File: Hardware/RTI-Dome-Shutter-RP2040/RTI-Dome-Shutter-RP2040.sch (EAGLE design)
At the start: 107 parts, among them IC2 24LC64T-I/SN, IC3 FT232RL, IC4 RASPBERRY_PI_PICO, IC8 REG1117-3.3V, IC9 REG1117-5V, J2 XT60PW-M, U1 W5500, X13 PN61729-S, X9 J1011F21PNL

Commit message: New RP2040 shutter board
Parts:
- removed 25MHZ: CB3LV-OSCILATOR, rti:CB3LV-OSCILATOR
- removed C10: 22nF, rcl:C-EUC0805
- removed C11, C12, C14, C16, C17, C20, C8, C9: 100nF, rcl:C-EUC0805
- removed C13, C18, C22: 10nF, rcl:C-EUC0805
- removed C15, C21: 6.8nF, rcl:C-EUC0805
- removed C19: 4.7uF, rcl:C-EUC0805
- removed FL1: BLM21AG121SN1D, BLM21AG121SN1D:BLM21AG121SN1D
- removed IC3: FT232RL, ftdichip:FT232RL
- removed R11: 10K, rcl:R-EU_R0805
- removed R23: 10 1%, rcl:R-EU_R0805
- removed R24, R25, R26, R27: 49.9 1%, rcl:R-EU_R0805
- removed R28, R29: 330, rcl:R-EU_R0805
- removed R30, R31, R32, R33, R34, R35, R36, R37, R38, R40: 4.7K, rcl:R-EU_R0805
- removed R39: 12.4K 1%, rcl:R-EU_R0805
- removed U$2: MCP120T, MCP120T:MCP120T
- removed U1: W5500, W5500:W5500
- removed X13: PN61729-S, rti:PN61729-S
- removed X9: J1011F21PNL, rti:J1011F21PNL
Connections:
- removed net ACT_LED: U1.ACTLED, X9.C-L
- removed net AVDD: C11.1, C12.1, C14.1, C17.1, FL1.1, R23.2, R24.2, R25.2, U1.AVDD@1, U1.AVDD@2, U1.AVDD@3, U1.AVDD@4, U1.AVDD@5, U1.AVDD@6
- removed net DTR_DSR_DCD: IC3.!DCD, IC3.!DSR, IC3.!DTR
- removed net INT_N: U1.INT_N
- removed net LINK_ACK: U1.LINKLED, X9.C-R
- removed net N$10: R28.1, X9.AL
- removed net N$11: C15.2, X9.RD+
- removed net N$12: C21.2, X9.RD-
- removed net N$13: C10.1, R23.1, X9.CT
- removed net N$17: U1.DUPLED
- removed net N$22: R31.1, U1.RSVD@2
- removed net N$23: R32.1, U1.RSVD@3
- removed net N$24: R33.1, U1.RSVD@4
- removed net N$25: R34.1, U1.RSVD@5
- removed net N$26: R35.1, U1.RSVD@6
- removed net N$27: R36.1, U1.PMODE2
- removed net N$28: R37.1, U1.PMODE1
- removed net N$29: R38.1, U1.PMODE0
- removed net N$31: C19.2, U1.TOCAP
- removed net N$32: U1.VBG
- removed net N$33: C18.2, U1.1V2O
- removed net N$34: R39.1, U1.EXRES1
- removed net N$35: R40.2, U1.RSVD@1
- removed net N$6: C8.1, IC3.3V3OUT
- removed net N$7: C22.1, R26.2, R27.2, X9.CR
- removed net N$8: R29.1, X9.A-R
- removed net RTS_CTS: IC3.!CTS, IC3.!RTS
- removed net RXN: C21.1, R26.1, U1.RXN
- removed net RXP: C15.1, R27.1, U1.RXP
- removed net TXN: R25.1, U1.TXN, X9.TD-
- removed net TXP: R24.1, U1.TXP, X9.TD+
- removed net USBD_N: IC3.USBDM, X13.2
- removed net USBD_P: IC3.USBDP, X13.3
- removed net USB_VCC: X13.1
- removed net XI: 25MHZ.FO, U1.XI/CLKIN
- removed net XO: U1.XO
- net 3.3V: no longer 25MHZ.OE, 25MHZ.VDD, C13.1, C16.1, C20.1, C9.1, FL1.2, IC3.VCCIO, R28.2, R29.2, R30.2, R36.2, R37.2, R38.2, U$2.VDD, U1.VDD
- net ETH_CS: no longer U1.SCS_N
- net ETH_RESET: no longer R30.1, U1.RST_N
- net FTDI_RESET: no longer IC3.!RESET, R11.1
- net GND: no longer 25MHZ.GND, C10.2, C11.2, C12.2, C13.2, C14.2, C16.2, C17.2, C18.1, C19.1, C20.2, C22.2, C8.2, C9.2, IC3.GND, IC3.GND@1, IC3.GND@2, IC3.GND@A, R11.2, R31.2, R32.2, R33.2, R34.2, R35.2, R39.2, R40.1, U$2.VSS, U1.AGND@1, U1.AGND@2, U1.AGND@3, U1.AGND@4, U1.AGND@5, U1.AGND@6, U1.GND, X13.4, X13.S1, X13.S2, X9.4/NC, X9.5/NC, X9.CGND, X9.CGND2
- net RESET: no longer U$2.~RST
- net RX2: no longer IC3.TXD
- net SCLK: no longer U1.SCLK
- net SDI: no longer U1.MISO
- net SDO: no longer U1.MOSI
- net TX2: no longer IC3.RXD
- net VCC: no longer IC3.VCC

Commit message: Switching to 0603 for resistor and capacitors
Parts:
- removed C7: 100nF, rcl:C-EUC0805
- C1, C23, C24, C27, C28, C3, C4, C40, C42, C43, C44, C45, C46, C5, C6: device rcl:C-EUC0805 -> rcl:C-EUC0603
- R1, R10, R12, R15, R16, R17, R18, R2, R20, R21, R22, R3, R4, R41, R44, R45, R46, R47, R49, R5, R50, R6, R7, R8, R9: device rcl:R-EU_R0805 -> rcl:R-EU_R0603
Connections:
- net GND: no longer C7.2
- net VCC: no longer C7.1

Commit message: Routed RP2040 Shutter board
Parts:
- C1, C23, C24, C27, C28, C3, C4, C40, C42, C43, C44, C45, C46, C5, C6: device rcl:C-EUC0603 -> rti:C-EU'0603'
- C41: device rcl:C-EUC0805 -> rti:C-EU'0603'
- IC2: device Microchip_By_element14_Batch_1:24LC64T-I/SN -> rti:24LC64T-I/SN
- R1, R10, R12, R15, R16, R17, R18, R2, R20, R21, R22, R3, R4, R41, R44, R45, R46, R47, R49, R5, R50, R6, R7, R8, R9: device rcl:R-EU_R0603 -> rti:R-EU'0603'
- R48: device rcl:R-EU_R0805 -> rti:R-EU'0603'

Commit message: Removed XBee from RP2040 Shutter controller
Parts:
- removed XB1: XBEE, rti:XBEE
- added Q1: DMG2305UX-7, samacsys:DMG2305UX-7
- added S1: EVQ-P2H02B, samacsys:EVQ-P2H02B
- IC4: value RASPBERRY_PI_PICO -> RASPBERRY_PI_PICOW; device samacsys:RASPBERRY_PI_PICO -> samacsys:RASPBERRY_PI_PICOW; DESCRIPTION RASPBERRY-PI - RASPBERRY PI PICO - Raspberry Pi Board, Rasp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 -> (none); MANUFACTURER_NAME RASPBERRY-PI PICO -> (none); MANUFACTURER_PART_NUMBER SC0916 -> (none); MOUSER_PART_NUMBER SC0915 -> (none); MPN SC0916 -> (none)
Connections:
- removed net N$64: IC4.VBUS
- removed net N$9: XB1.!CTS!/DIO7, XB1.!RTS!/AD6/DIO6
- new net VBUS: IC4.VBUS, Q1.G
- new net VSYS: IC4.VSYS, Q1.S
- net 3.3V: no longer XB1.VCC
- net GND: now also S1.COM_1, S1.COM_2; no longer XB1.!DTR!/SLEEP_RQ/DI8, XB1.GND
- net RESET: now also S1.NO_2
- net VCC: now also Q1.D; no longer IC4.VSYS
- net XBEE_DIN: no longer XB1.DIN/!CONFIG
- net XBEE_DOUT: no longer XB1.DOUT
- net XBEE_RESET: no longer XB1.!RESET

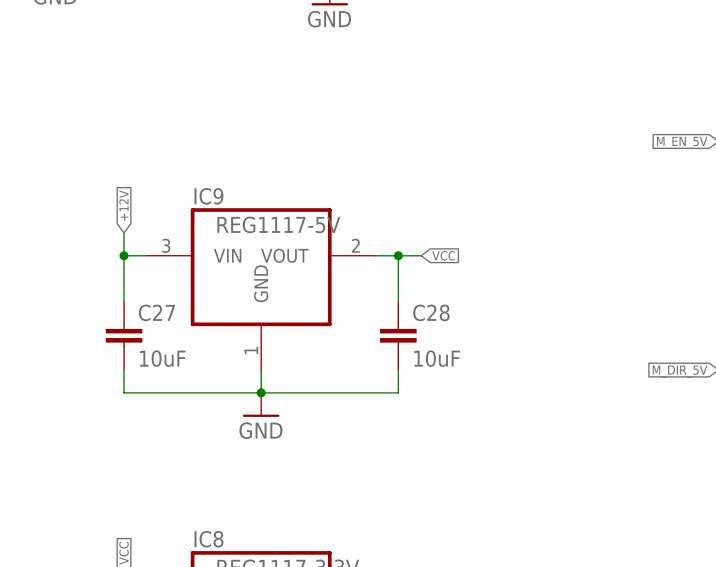
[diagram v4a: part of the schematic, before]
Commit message: Removed XBee from RP2040 boards as they'll use WiFi
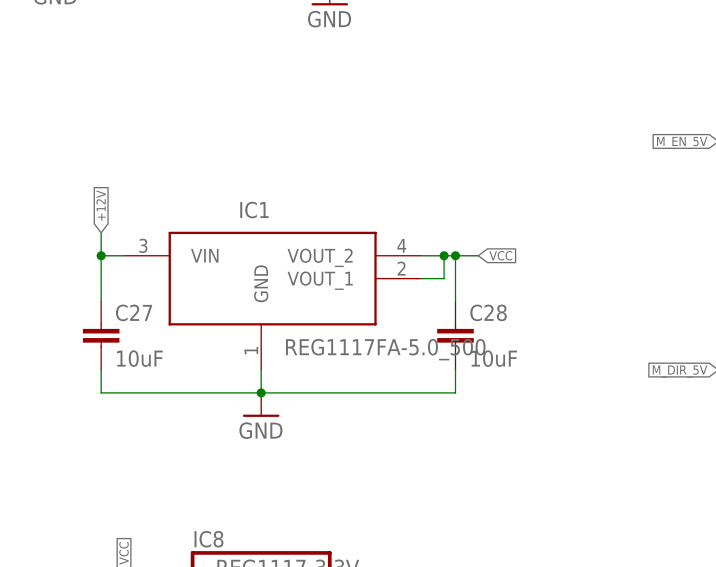
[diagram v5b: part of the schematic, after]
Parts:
- removed IC9: REG1117-5V, burr-brown:REG1117
- added IC1: REG1117FA-5.0_500, REG1117FA-5.0_500:REG1117FA-5.0_500
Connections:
- net +12V: now also IC1.VIN; no longer IC9.VIN
- net GND: now also IC1.GND; no longer IC9.GND
- net VCC: now also IC1.VOUT_1, IC1.VOUT_2; no longer IC9.VOUT
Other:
- moved on the sheet: C27, C28
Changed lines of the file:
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@@
 </part>
 <part name="GND22" library="supply1" library_urn="urn:adsk.eagle:library:371" deviceset="GND" device=""/>
-<part name="IC9" library="burr-brown" library_urn="urn:adsk.eagle:library:37504555" deviceset="REG1117" device="" package3d_urn="urn:adsk.eagle:package:37504714/1" value="REG1117-5V">
-<attribute name="MPN" value="REG1117-3.3/2K5"/>
-</part>
 <part name="C27" library="rti" library_urn="urn:adsk.eagle:library:37256580" deviceset="C-EU" device="'0603'" package3d_urn="urn:adsk.eagle:package:41513588/2" value="10uF">
 <spice>
@@
 <part name="S1" library="samacsys" library_urn="urn:adsk.eagle:library:37256869" deviceset="EVQ-P2H02B" device="" package3d_urn="urn:adsk.eagle:package:44159643/2"/>
 <part name="GND3" library="supply1" library_urn="urn:adsk.eagle:library:371" deviceset="GND" device=""/>
+<part name="IC1" library="REG1117FA-5.0_500" library_urn="urn:adsk.eagle:library:43937876" deviceset="REG1117FA-5.0_500" device="" package3d_urn="urn:adsk.eagle:package:43937879/3"/>
 </parts>
 <sheets>
@@
 <attribute name="VALUE" x="27.94" y="93.98" size="1.778" layer="96"/>
 </instance>
-<instance part="IC9" gate="G$1" x="30.48" y="152.4" smashed="yes">
-<attribute name="NAME" x="22.86" y="158.115" size="1.778" layer="95" ratio="10"/>
-<attribute name="VALUE" x="25.4" y="154.94" size="1.778" layer="96" ratio="10"/>
-</instance>
-<instance part="C27" gate="G$1" x="15.24" y="144.78" smashed="yes">
-<attribute name="MPN" x="15.24" y="144.78" size="1.778" layer="96" display="off"/>
-<attribute name="NAME" x="16.764" y="145.161" size="1.778" layer="95"/>
-<attribute name="VALUE" x="16.764" y="140.081" size="1.778" layer="96"/>
-</instance>
-<instance part="C28" gate="G$1" x="45.72" y="144.78" smashed="yes">
-<attribute name="MPN" x="45.72" y="144.78" size="1.778" layer="96" display="off"/>
-<attribute name="NAME" x="47.244" y="145.161" size="1.778" layer="95"/>
-<attribute name="VALUE" x="47.244" y="140.081" size="1.778" layer="96"/>
+<instance part="C27" gate="G$1" x="12.7" y="144.78" smashed="yes">
+<attribute name="MPN" x="12.7" y="144.78" size="1.778" layer="96" display="off"/>
+<attribute name="NAME" x="14.224" y="145.161" size="1.778" layer="95"/>
+<attribute name="VALUE" x="14.224" y="140.081" size="1.778" layer="96"/>
+</instance>
+<instance part="C28" gate="G$1" x="52.07" y="144.78" smashed="yes">
+<attribute name="MPN" x="52.07" y="144.78" size="1.778" layer="96" display="off"/>
+<attribute name="NAME" x="53.594" y="145.161" size="1.778" layer="95"/>
+<attribute name="VALUE" x="53.594" y="140.081" size="1.778" layer="96"/>
 </instance>
 <instance part="GND23" gate="1" x="30.48" y="134.62" smashed="yes">
@@
 <instance part="GND3" gate="1" x="219.71" y="30.48" smashed="yes">
 <attribute name="VALUE" x="217.17" y="27.94" size="1.778" layer="96"/>
+</instance>
+<instance part="IC1" gate="G$1" x="15.24" y="152.4" smashed="yes">
+<attribute name="NAME" x="27.94" y="157.48" size="1.778" layer="95" align="center-left"/>
+<attribute name="VALUE" x="33.02" y="142.24" size="1.778" layer="96" align="center-left"/>
 </instance>
 </instances>
@@
 </segment>
 <segment>
-<pinref part="IC9" gate="G$1" pin="GND"/>
 <wire x1="30.48" y1="137.16" x2="30.48" y2="139.7" width="0.1524" layer="91"/>
 <pinref part="C28" gate="G$1" pin="2"/>
-<wire x1="45.72" y1="139.7" x2="45.72" y2="137.16" width="0.1524" layer="91"/>
-<wire x1="45.72" y1="137.16" x2="30.48" y2="137.16" width="0.1524" layer="91"/>
+<wire x1="52.07" y1="139.7" x2="52.07" y2="137.16" width="0.1524" layer="91"/>
+<wire x1="52.07" y1="137.16" x2="30.48" y2="137.16" width="0.1524" layer="91"/>
 <junction x="30.48" y="137.16"/>
 <pinref part="C27" gate="G$1" pin="2"/>
-<wire x1="15.24" y1="139.7" x2="15.24" y2="137.16" width="0.1524" layer="91"/>
-<wire x1="15.24" y1="137.16" x2="30.48" y2="137.16" width="0.1524" layer="91"/>
+<wire x1="12.7" y1="139.7" x2="12.7" y2="137.16" width="0.1524" layer="91"/>
+<wire x1="12.7" y1="137.16" x2="30.48" y2="137.16" width="0.1524" layer="91"/>
 <pinref part="GND23" gate="1" pin="GND"/>
+<pinref part="IC1" gate="G$1" pin="GND"/>
 </segment>
 <segment>
@@
 <segment>
 <pinref part="C27" gate="G$1" pin="1"/>
-<pinref part="IC9" gate="G$1" pin="VIN"/>
-<wire x1="15.24" y1="147.32" x2="15.24" y2="152.4" width="0.1524" layer="91"/>
-<wire x1="15.24" y1="152.4" x2="17.78" y2="152.4" width="0.1524" layer="91"/>
-<wire x1="15.24" y1="154.94" x2="15.24" y2="152.4" width="0.1524" layer="91"/>
-<junction x="15.24" y="152.4"/>
-<label x="15.24" y="154.94" size="1.016" layer="95" rot="R90" xref="yes"/>
+<wire x1="12.7" y1="147.32" x2="12.7" y2="152.4" width="0.1524" layer="91"/>
+<wire x1="12.7" y1="152.4" x2="15.24" y2="152.4" width="0.1524" layer="91"/>
+<wire x1="12.7" y1="154.94" x2="12.7" y2="152.4" width="0.1524" layer="91"/>
+<junction x="12.7" y="152.4"/>
+<label x="12.7" y="154.94" size="1.016" layer="95" rot="R90" xref="yes"/>
+<pinref part="IC1" gate="G$1" pin="VIN"/>
 </segment>
 </net>
@@
 </segment>
 <segment>
-<pinref part="IC9" gate="G$1" pin="VOUT"/>
 <pinref part="C28" gate="G$1" pin="1"/>
-<wire x1="43.18" y1="152.4" x2="45.72" y2="152.4" width="0.1524" layer="91"/>
-<wire x1="45.72" y1="152.4" x2="45.72" y2="147.32" width="0.1524" layer="91"/>
-<wire x1="48.26" y1="152.4" x2="45.72" y2="152.4" width="0.1524" layer="91"/>
-<junction x="45.72" y="152.4"/>
-<label x="48.26" y="152.4" size="1.016" layer="95" ratio="4" xref="yes"/>
-</segment>
-<segment>
+<wire x1="52.07" y1="152.4" x2="52.07" y2="147.32" width="0.1524" layer="91"/>
+<wire x1="54.61" y1="152.4" x2="52.07" y2="152.4" width="0.1524" layer="91"/>
+<label x="54.61" y="152.4" size="1.016" layer="95" ratio="4" xref="yes"/>
+<pinref part="IC1" gate="G$1" pin="VOUT_2"/>
+<wire x1="48.26" y1="152.4" x2="50.8" y2="152.4" width="0.1524" layer="91"/>
+<junction x="52.07" y="152.4"/>
+<pinref part="IC1" gate="G$1" pin="VOUT_1"/>
+<wire x1="50.8" y1="152.4" x2="52.07" y2="152.4" width="0.1524" layer="91"/>
+<wire x1="48.26" y1="149.86" x2="50.8" y2="149.86" width="0.1524" layer="91"/>
+<wire x1="50.8" y1="149.86" x2="50.8" y2="152.4" width="0.1524" layer="91"/>
+<junction x="50.8" y="152.4"/>
+</segment>
+<segment>
